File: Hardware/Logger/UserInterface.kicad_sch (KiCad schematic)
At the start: 15 parts, among them SW1 SW_Push, SW2 SW_Push, SW3 SW_Push, SW4 SW_Push, U2 ST7735S

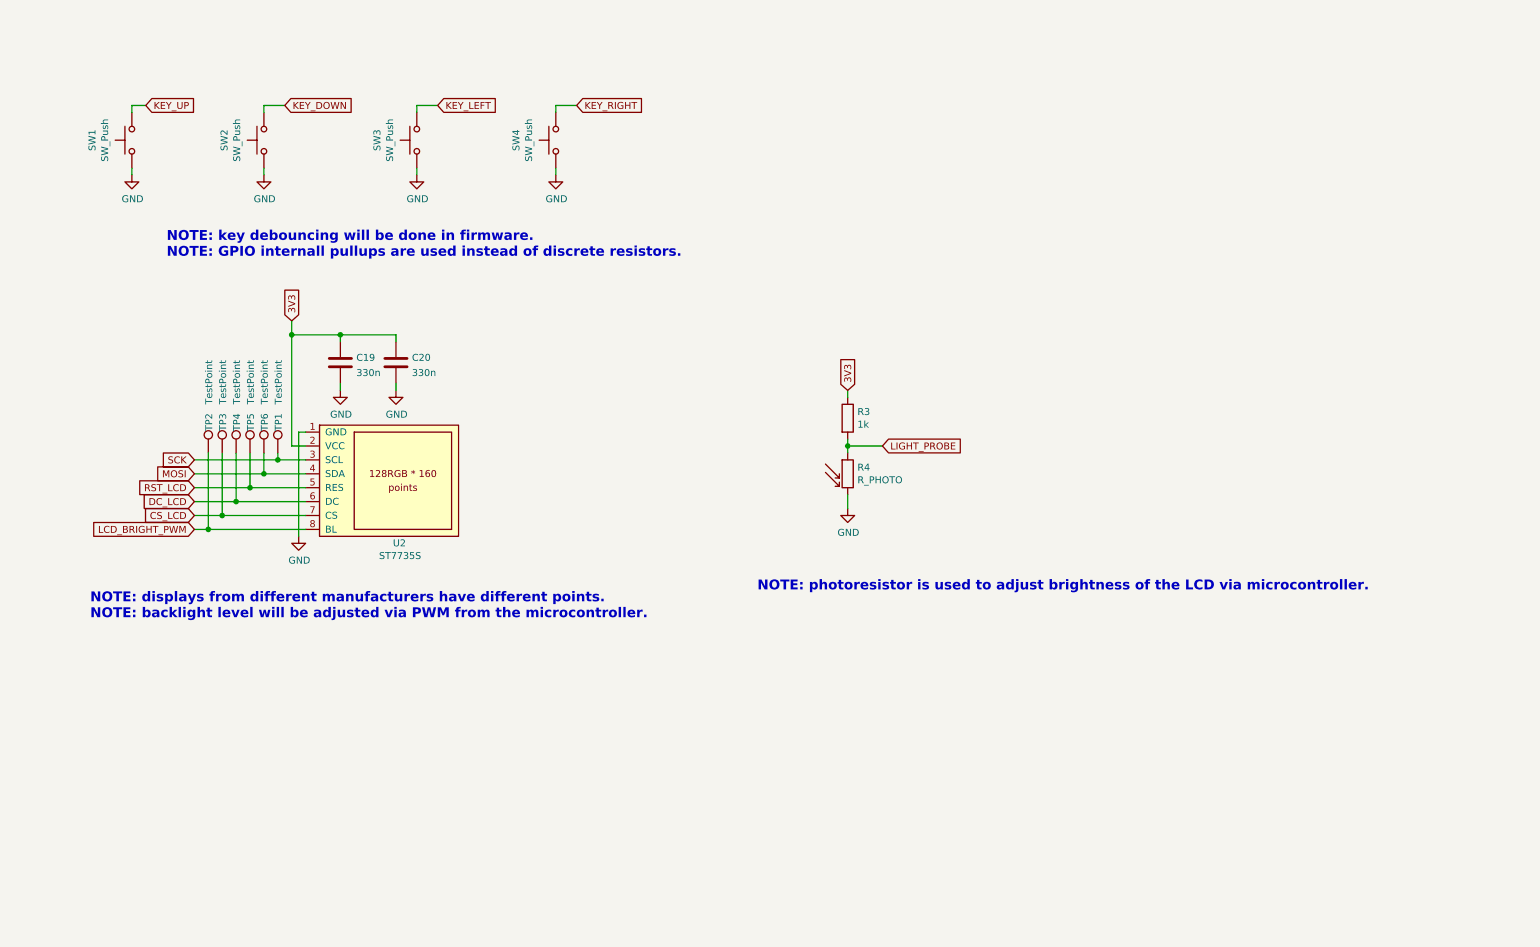
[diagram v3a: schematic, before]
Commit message: apply actual gpio connections to stm32 board, changed photoresistor to phototransistor
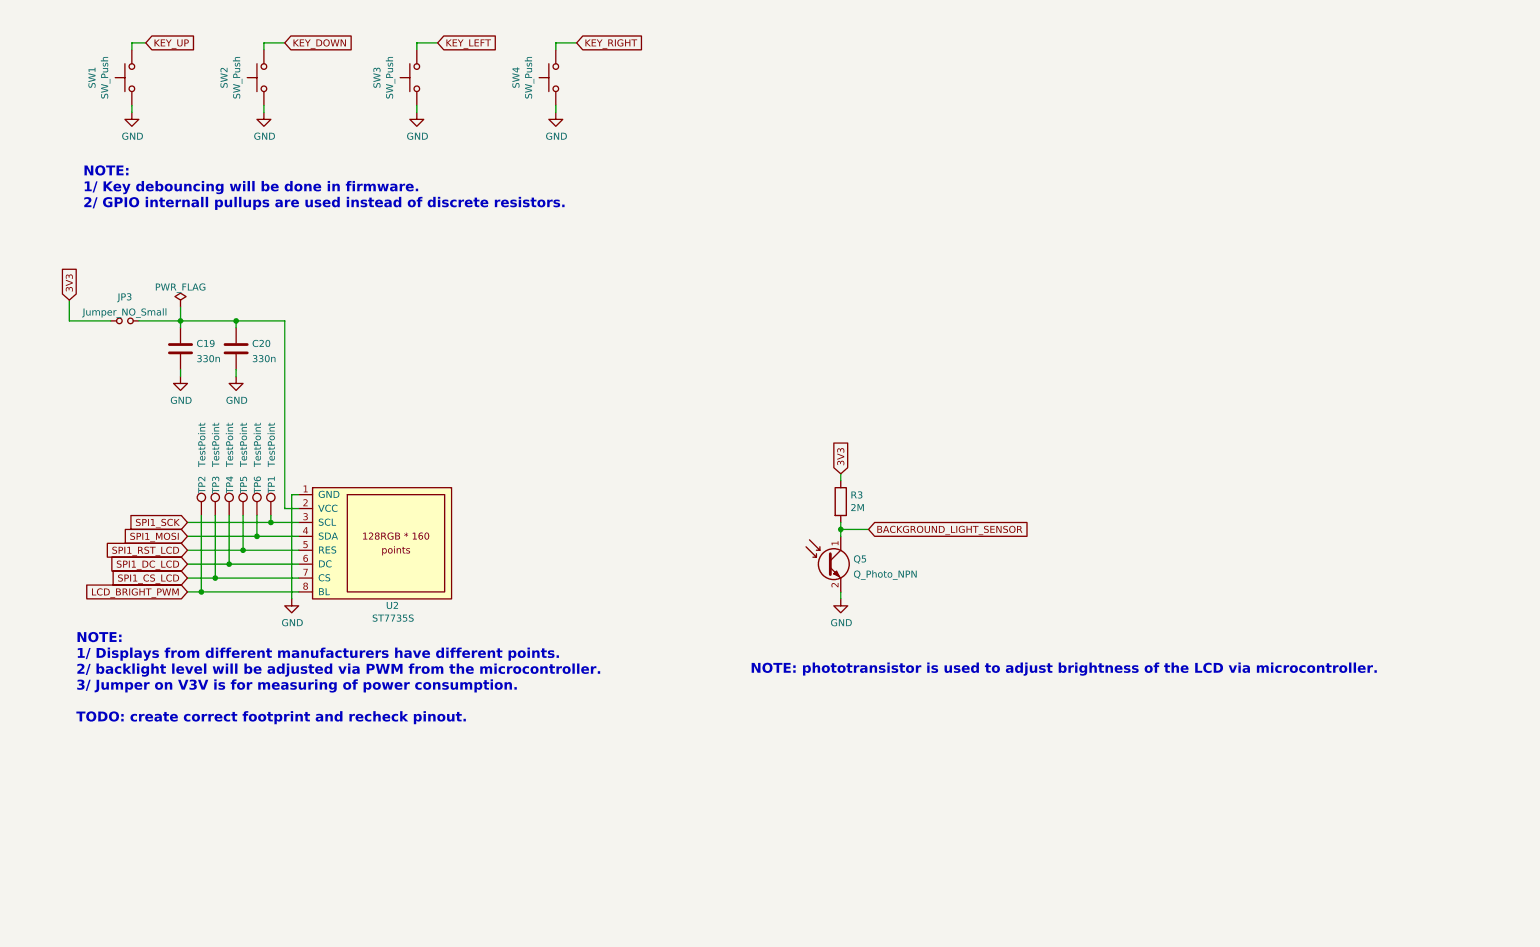
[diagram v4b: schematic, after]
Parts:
- removed R4: R_PHOTO, OptoDevice:R_LDR_7x6mm_P5.1mm_Vertical, symbol Device:R_PHOTO
- added JP3: Jumper_NO_Small, symbol Device:Jumper_NO_Small
- added Q5: Q_Photo_NPN, symbol Device:Q_Photo_NPN
- R3: value 1k -> 2M
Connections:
- net 3V3: now also JP3.1; no longer C19.1, C20.1, U2.2 (VCC)
- net GND: now also Q5.2 (E)
- net CS_LCD renamed SPI1_CS_LCD
- net DC_LCD renamed SPI1_DC_LCD
- net LIGHT_PROBE renamed BACKGROUND_LIGHT_SENSOR
- net BACKGROUND_LIGHT_SENSOR: now also Q5.1 (C)
- net MOSI renamed SPI1_MOSI
- net RST_LCD renamed SPI1_RST_LCD
- net SCK renamed SPI1_SCK
- new net: C19.1, C20.1, JP3.2, U2.2 (VCC)
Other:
- note added: "NOTE: 1/ Displays from different manufacturers have different points. 2/ backlight level will be adjusted via PWM from the microcontroller. 3/ Jumper on V3V is for measuring of power consumption. TODO: create correct footprint and recheck pinout."
- note added: "NOTE: 1/ Key debouncing will be done in firmware. 2/ GPIO internall pullups are used instead of discrete resistors."
- note added: "NOTE: phototransistor is used to adjust brightness of the LCD via microcontroller."
- note removed: "NOTE: displays from different manufacturers have different points. NOTE: backlight level will be adjusted via PWM from the microcontroller."
- note removed: "NOTE: key debouncing will be done in firmware. NOTE: GPIO internall pullups are used instead of discrete resistors."
- note removed: "NOTE: photoresistor is used to adjust brightness of the LCD via microcontroller."
- moved on the sheet: C19, C20, R3, SW1, SW2, SW3, SW4, TP1, TP2, TP3, TP4, TP5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

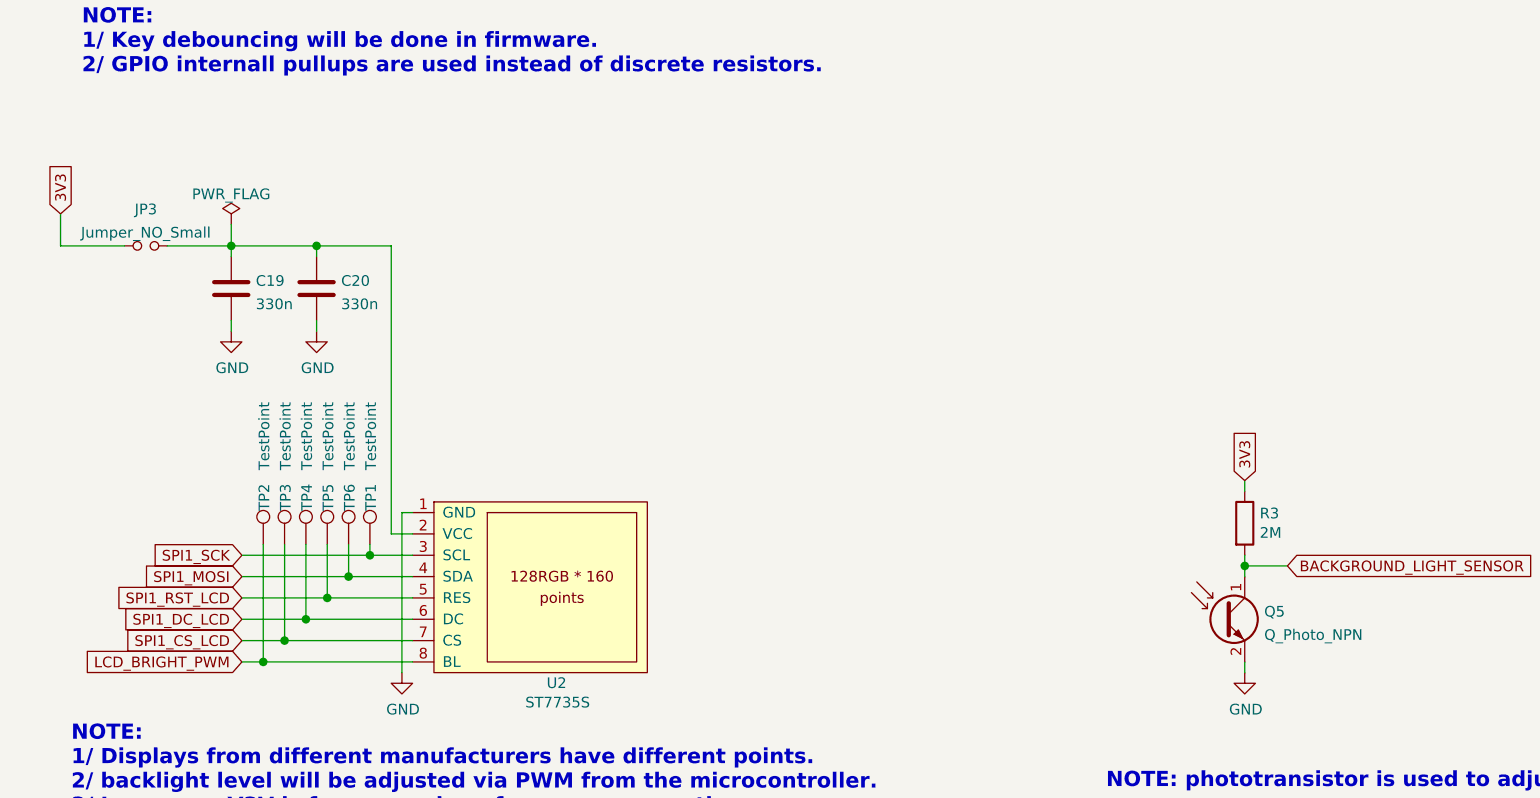
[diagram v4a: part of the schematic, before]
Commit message: draft of rev 3.0, cleanup of repo from not fully open source libs
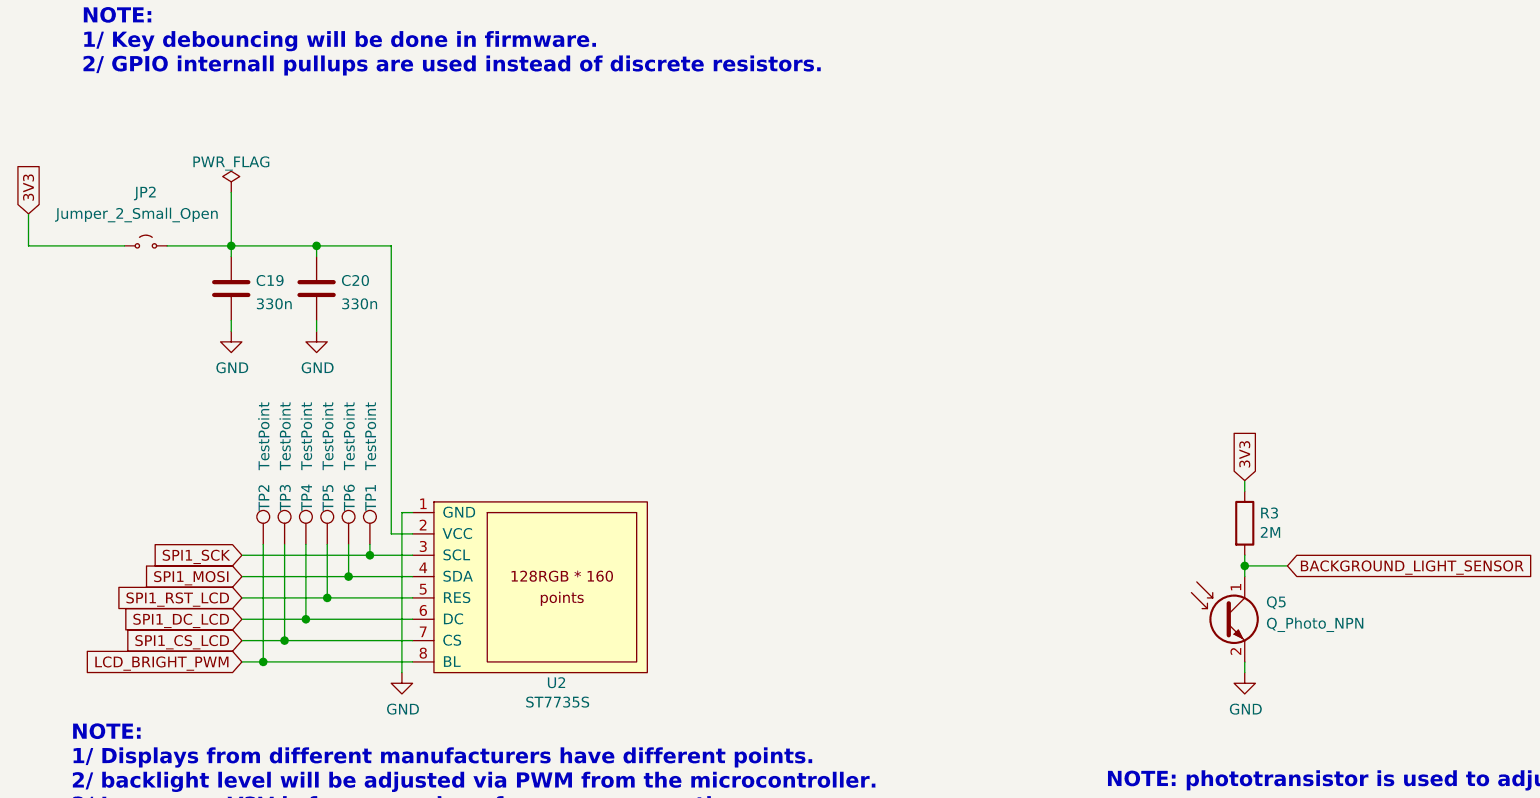
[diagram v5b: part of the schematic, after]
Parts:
- removed JP3: Jumper_NO_Small, symbol Device:Jumper_NO_Small
- added JP2: Jumper_2_Small_Open, Jumper:SolderJumper-2_P1.3mm_Open_TrianglePad1.0x1.5mm, symbol Jumper:Jumper_2_Small_Open
- Q5: footprint (none) -> Package_TO_SOT_THT:TO-5-2
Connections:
- net 3V3: now also JP2.1 (A)
- net at C19.1, C20.1, U2.2 (VCC): now also JP2.2 (B)
